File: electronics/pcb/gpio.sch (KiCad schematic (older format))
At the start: 31 parts, among them J1 Micro_SD_Card_Det_Hirose_DM3AT, J2 USB_A, J3 USB_A, J5 Conn_02x10_Odd_Even, U2 A33, Y1 24Mhz, Y2 32.768khz

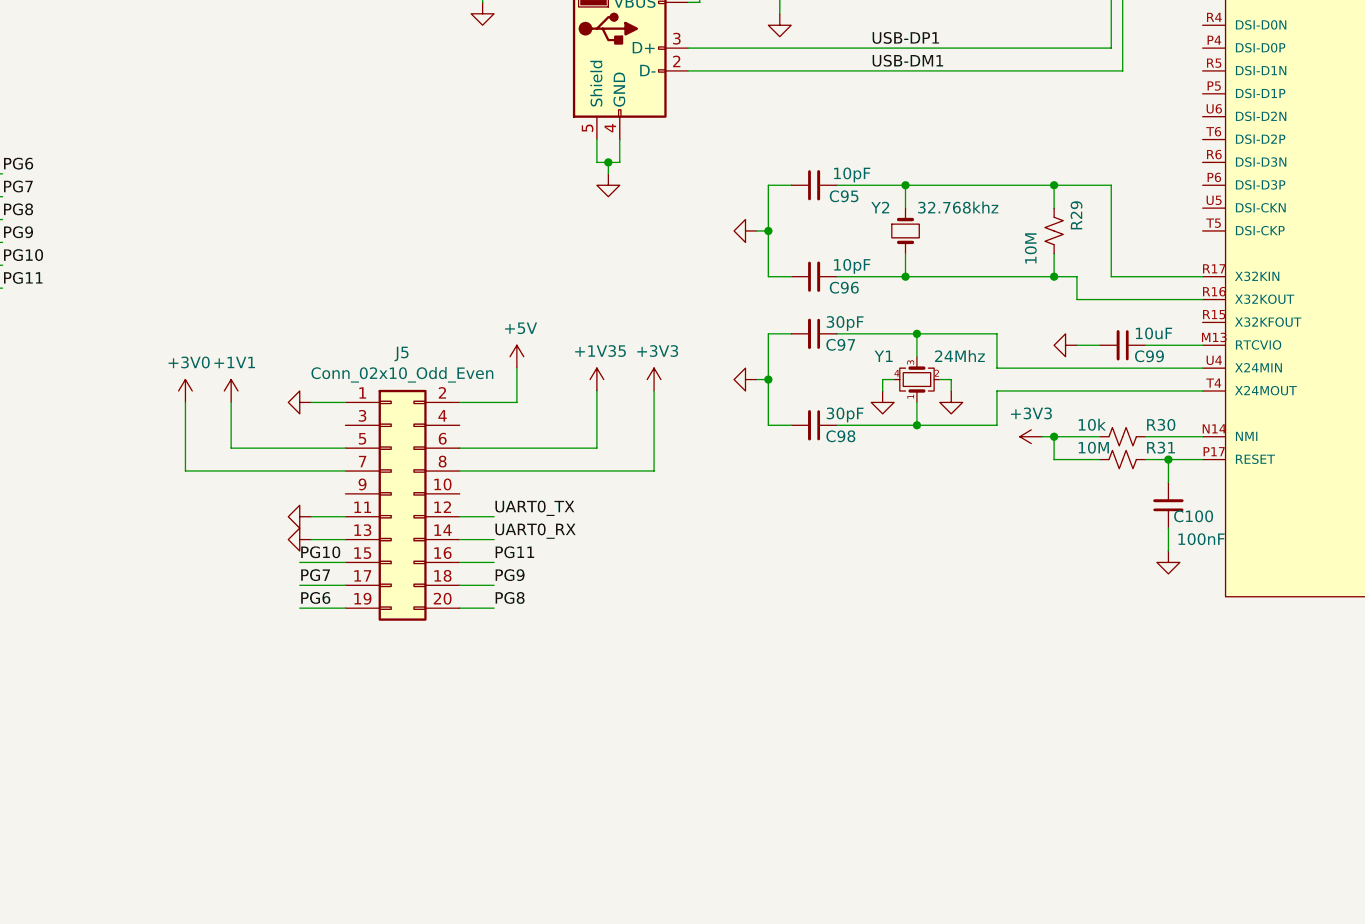
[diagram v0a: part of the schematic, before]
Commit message: Pulled out reset line
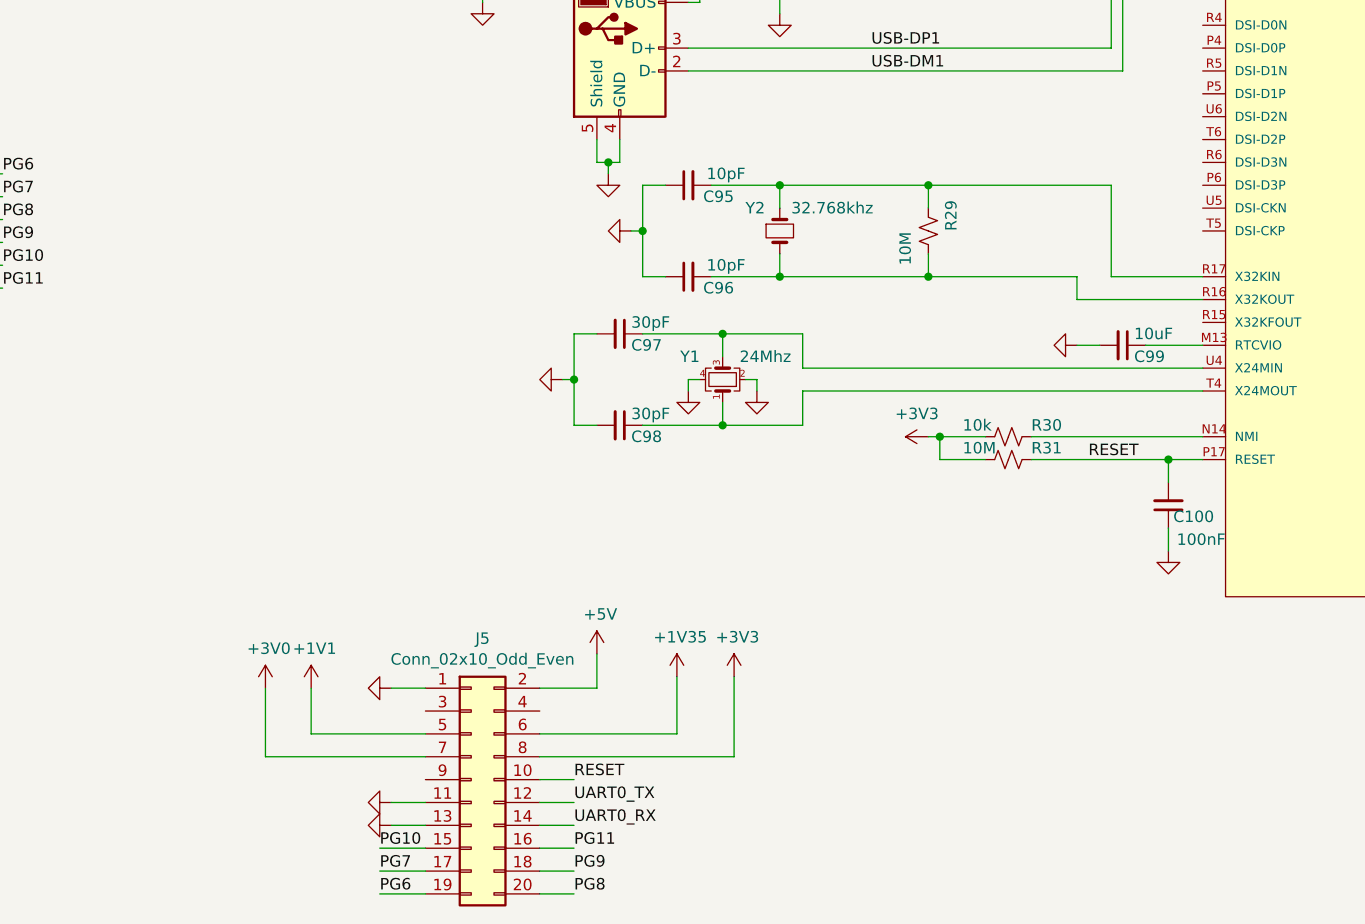
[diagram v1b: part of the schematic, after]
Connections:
- net RESET: now reaches C100.2, R31.1, U2.P17 (RESET)
- net RESET: now also J5.10 (Pin_10)
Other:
- moved on the sheet: C95, C96, C97, C98, J5, R29, R30, R31, Y1, Y2

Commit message: DRC + BOM script
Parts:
- J1: MPN (none) -> DM3AT-SF-PEJM5
- J2, J3: MPN (none) -> 1050570001; Part Number 1050570001 -> (none)
- Y1: MPN (none) -> ABM8G-24.000MHZ-18-D2Y-T; Part Number ABM8G-24.000MHZ-18-D2Y-T -> (none)
- Y2: MPN (none) -> ABS05-32.768KHZ-9-T; Part Number ABS05-32.768KHZ-9-T -> (none)
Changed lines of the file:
@@
 F 2 "Connector_Card:microSD_HC_Hirose_DM3AT-SF-PEJM5" H 12000 2150 50  0001 C CNN
 F 3 "https://www.hirose.com/product/en/download_file/key_name/DM3/category/Catalog/doc_file_id/49662/?file_category_id=4&item_id=195&is_series=1" H 9950 1550 50  0001 C CNN
+F 4 "DM3AT-SF-PEJM5" H 9950 1450 50  0001 C CNN "MPN"
 	1    9950 1450
 	1    0    0    -1
@@
 F 2 "Crystal:Crystal_SMD_Abracon_ABM8G-4Pin_3.2x2.5mm" H 5950 5050 50  0001 C CNN
 F 3 "~" H 5950 5050 50  0001 C CNN
-F 4 "ABM8G-24.000MHZ-18-D2Y-T" H 5950 5050 50  0001 C CNN "Part Number"
+F 4 "ABM8G-24.000MHZ-18-D2Y-T" H 5950 5050 50  0001 C CNN "MPN"
 	1    5950 5050
 	0    -1   -1   0
@@
 F 2 "Abracon:Abracon-ABS05-0-0-MFG" H 6200 4400 50  0001 C CNN
 F 3 "~" H 6200 4400 50  0001 C CNN
-F 4 "ABS05-32.768KHZ-9-T" H 6200 4400 50  0001 C CNN "Part Number"
+F 4 "ABS05-32.768KHZ-9-T" H 6200 4400 50  0001 C CNN "MPN"
 	1    6200 4400
 	0    1    1    0
@@
 F 2 "Connector_USB:USB_A_Molex_105057_Vertical" H 5100 2800 50  0001 C CNN
 F 3 " ~" H 5100 2800 50  0001 C CNN
-F 4 "1050570001" H 4950 2850 50  0001 C CNN "Part Number"
+F 4 "1050570001" H 4950 2850 50  0001 C CNN "MPN"
 	1    4950 2850
 	1    0    0    -1
@@
 F 2 "Connector_USB:USB_A_Molex_105057_Vertical" H 5650 3550 50  0001 C CNN
 F 3 " ~" H 5650 3550 50  0001 C CNN
-F 4 "1050570001" H 5500 3600 50  0001 C CNN "Part Number"
+F 4 "1050570001" H 5500 3600 50  0001 C CNN "MPN"
 	1    5500 3600
 	1    0    0    -1

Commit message: Removed all the extra fields
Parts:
- U2: DC Supply Voltage for I/O 1.8V ~ 3.3V -> (none); category IC -> (none); ipc land pattern name BGA289N80P17X17_1400X1400X129 -> (none); lead free yes -> (none); library id f6b937119e25c27a -> (none); manufacturer Allwinner Technology Co., Ltd. -> (none); package TFBGA282 -> (none); rohs yes -> (none); temperature range high +125°C -> (none); temperature range low -40°C -> (none)
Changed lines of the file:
@@
 F 2 "A33_FP:Allwinner_Technology_Co.,_Ltd.-A33-0" H 1650 1350 50  0001 L CNN
 F 3 "http://dl.linux-sunxi.org/A33/A33_Datasheet_release1.0.pdf" H 1650 1450 50  0001 L CNN
-F 4 "1.8V ~ 3.3V" H 1650 1550 50  0001 L CNN "DC Supply Voltage for I/O"
-F 5 "IC" H 1650 1650 50  0001 L CNN "category"
-F 6 "BGA289N80P17X17_1400X1400X129" H 1650 1750 50  0001 L CNN "ipc land pattern name"
-F 7 "yes" H 1650 1850 50  0001 L CNN "lead free"
-F 8 "f6b937119e25c27a" H 1650 1950 50  0001 L CNN "library id"
-F 9 "Allwinner Technology Co., Ltd." H 1650 2050 50  0001 L CNN "manufacturer"
-F 10 "TFBGA282" H 1650 2150 50  0001 L CNN "package"
-F 11 "yes" H 1650 2250 50  0001 L CNN "rohs"
-F 12 "+125°C" H 1650 2350 50  0001 L CNN "temperature range high"
-F 13 "-40°C" H 1650 2450 50  0001 L CNN "temperature range low"
-F 14 "" H 1650 2550 50  0001 L CNN "voltage"
 	3    1650 950
 	1    0    0    -1
@@
 F 2 "A33_FP:Allwinner_Technology_Co.,_Ltd.-A33-0" H 7950 3400 50  0001 L CNN
 F 3 "http://dl.linux-sunxi.org/A33/A33_Datasheet_release1.0.pdf" H 7950 3500 50  0001 L CNN
-F 4 "1.8V ~ 3.3V" H 7950 3600 50  0001 L CNN "DC Supply Voltage for I/O"
-F 5 "IC" H 7950 3700 50  0001 L CNN "category"
-F 6 "BGA289N80P17X17_1400X1400X129" H 7950 3800 50  0001 L CNN "ipc land pattern name"
-F 7 "yes" H 7950 3900 50  0001 L CNN "lead free"
-F 8 "f6b937119e25c27a" H 7950 4000 50  0001 L CNN "library id"
-F 9 "Allwinner Technology Co., Ltd." H 7950 4100 50  0001 L CNN "manufacturer"
-F 10 "TFBGA282" H 7950 4200 50  0001 L CNN "package"
-F 11 "yes" H 7950 4300 50  0001 L CNN "rohs"
-F 12 "+125°C" H 7950 4400 50  0001 L CNN "temperature range high"
-F 13 "-40°C" H 7950 4500 50  0001 L CNN "temperature range low"
-F 14 "" H 7950 4600 50  0001 L CNN "voltage"
 	4    7950 3000
 	1    0    0    -1

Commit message: Part numbers are _properly_ in now.
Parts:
- C100, C104, C93: MPN (none) -> CC0402KRX7R7BB104
- C101: MPN (none) -> CL05A105KO5NNNC
- C102, C103, C105, C106, C99: MPN (none) -> CL05A106MQ5NUNC
- C94: MPN (none) -> GRM155R60J226ME11D
- C95, C96: MPN (none) -> CC0402JRNPO9BN100
- C97, C98: MPN (none) -> CC0402JRNPO9BN300
- R20, R21, R23, R24, R25: MPN (none) -> CR0402-JW-104GLF
- R22, R30: MPN (none) -> RC0402JR-0710KL
- R29, R31: MPN (none) -> 0402WGJ0106TCE
- R32: MPN (none) -> RC0402FR-07200KL
- U2: MPN (none) -> A33
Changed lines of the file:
@@
 F 1 "A33" H 2200 1124 50 0000 C CNN
 F 2 "A33_FP:Allwinner_Technology_Co.,_Ltd.-A33-0" H 1650 1350 50 0001 L CNN
-F 3 "http://dl.linux-sunxi.org/A33/A33_Datasheet_release1.0.pdf" H 1650 1450 50 0001 L CNN
+F 3 "~" H 1650 1450 50 0001 L CNN
+F 4 "A33" H 2200 1315 50 0001 C CNN "MPN"
+F 5 "~" H 2200 1315 50 0001 C CNN "Tolerance"
 	3    1650 950
 	1    0    0    -1
@@
 F 1 "A33" H 8850 3174 50 0000 C CNN
 F 2 "A33_FP:Allwinner_Technology_Co.,_Ltd.-A33-0" H 7950 3400 50 0001 L CNN
-F 3 "http://dl.linux-sunxi.org/A33/A33_Datasheet_release1.0.pdf" H 7950 3500 50 0001 L CNN
+F 3 "~" H 7950 3500 50 0001 L CNN
+F 4 "A33" H 8850 3365 50 0001 C CNN "MPN"
+F 5 "~" H 8850 3365 50 0001 C CNN "Tolerance"
 	4    7950 3000
 	1    0    0    -1
@@
 F 1 "Micro_SD_Card_Det_Hirose_DM3AT" H 9900 2176 50 0000 C CNN
 F 2 "Connector_Card:microSD_HC_Hirose_DM3AT-SF-PEJM5" H 12000 2150 50 0001 C CNN
-F 3 "https://www.hirose.com/product/en/download_file/key_name/DM3/category/Catalog/doc_file_id/49662/?file_category_id=4&item_id=195&is_series=1" H 9950 1550 50 0001 C CNN
+F 3 "~" H 9950 1550 50 0001 C CNN
 F 4 "DM3AT-SF-PEJM5" H 9950 1450 50 0001 C CNN "MPN"
+F 5 "~" H 9900 2367 50 0001 C CNN "Tolerance"
 	1    9950 1450
 	1    0    0    -1
@@
 F 2 "Resistor_SMD:R_0402_1005Metric" H 8200 1650 50 0001 C CNN
 F 3 "~" H 8200 1650 50 0001 C CNN
+F 4 "CR0402-JW-104GLF" H 8150 1800 50 0001 C CNN "MPN"
+F 5 "~" H 8150 1800 50 0001 C CNN "Tolerance"
 	1    8200 1650
 	0    -1   -1   0
@@
 F 2 "Resistor_SMD:R_0402_1005Metric" H 8200 1750 50 0001 C CNN
 F 3 "~" H 8200 1750 50 0001 C CNN
+F 4 "CR0402-JW-104GLF" H 8150 1900 50 0001 C CNN "MPN"
+F 5 "~" H 8150 1900 50 0001 C CNN "Tolerance"
 	1    8200 1750
 	0    -1   -1   0
@@
 F 2 "Resistor_SMD:R_0402_1005Metric" H 8200 1150 50 0001 C CNN
 F 3 "~" H 8200 1150 50 0001 C CNN
+F 4 "CR0402-JW-104GLF" H 8150 1300 50 0001 C CNN "MPN"
+F 5 "~" H 8150 1300 50 0001 C CNN "Tolerance"
 	1    8200 1150
 	0    -1   -1   0
@@
 F 2 "Resistor_SMD:R_0402_1005Metric" H 8200 1050 50 0001 C CNN
 F 3 "~" H 8200 1050 50 0001 C CNN
+F 4 "CR0402-JW-104GLF" H 8150 1200 50 0001 C CNN "MPN"
+F 5 "~" H 8150 1200 50 0001 C CNN "Tolerance"
 	1    8200 1050
 	0    -1   -1   0
@@
 F 2 "Resistor_SMD:R_0402_1005Metric" H 8200 1250 50 0001 C CNN
 F 3 "~" H 8200 1250 50 0001 C CNN
+F 4 "RC0402JR-0710KL" H 8150 1400 50 0001 C CNN "MPN"
+F 5 "~" H 8150 1400 50 0001 C CNN "Tolerance"
 	1    8200 1250
 	0    -1   -1   0
@@
 F 2 "Resistor_SMD:R_0402_1005Metric" H 8200 1850 50 0001 C CNN
 F 3 "~" H 8200 1850 50 0001 C CNN
+F 4 "CR0402-JW-104GLF" H 8150 2000 50 0001 C CNN "MPN"
+F 5 "~" H 8150 2000 50 0001 C CNN "Tolerance"
 	1    8200 1850
 	0    -1   -1   0
@@
 F 2 "Capacitor_SMD:C_0402_1005Metric" H 7500 1300 50 0001 C CNN
 F 3 "~" H 7500 1300 50 0001 C CNN
+F 4 "CC0402KRX7R7BB104" H 7550 1450 50 0001 C CNN "MPN"
+F 5 "~" H 7550 1450 50 0001 C CNN "Tolerance"
 	1    7500 1300
 	1    0    0    -1
@@
 F 2 "Capacitor_SMD:C_0402_1005Metric" H 7700 1300 50 0001 C CNN
 F 3 "~" H 7700 1300 50 0001 C CNN
+F 4 "GRM155R60J226ME11D" H 7750 1450 50 0001 C CNN "MPN"
+F 5 "~" H 7750 1450 50 0001 C CNN "Tolerance"
 	1    7700 1300
 	1    0    0    -1
@@
 F 3 "~" H 5950 5050 50 0001 C CNN
 F 4 "ABM8G-24.000MHZ-18-D2Y-T" H 5950 5050 50 0001 C CNN "MPN"
+F 5 "~" H 6050 5250 50 0001 C CNN "Tolerance"
 	1    5950 5050
 	0    -1   -1   0
@@
 F 3 "~" H 6200 4400 50 0001 C CNN
 F 4 "ABS05-32.768KHZ-9-T" H 6200 4400 50 0001 C CNN "MPN"
+F 5 "~" H 6100 4350 50 0001 C CNN "Tolerance"
 	1    6200 4400
 	0    1    1    0
@@
 F 2 "Capacitor_SMD:C_0402_1005Metric" H 5500 4850 50 0001 C CNN
 F 3 "~" H 5500 4850 50 0001 C CNN
+F 4 "CC0402JRNPO9BN300" H 5550 5000 50 0001 C CNN "MPN"
+F 5 "~" H 5550 5000 50 0001 C CNN "Tolerance"
 	1    5500 4850
 	0    1    1    0
@@
 F 2 "Capacitor_SMD:C_0402_1005Metric" H 5500 5250 50 0001 C CNN
 F 3 "~" H 5500 5250 50 0001 C CNN
+F 4 "CC0402JRNPO9BN300" H 5550 5400 50 0001 C CNN "MPN"
+F 5 "~" H 5550 5400 50 0001 C CNN "Tolerance"
 	1    5500 5250
 	0    1    1    0
@@
 F 2 "Capacitor_SMD:C_0402_1005Metric" H 5800 4600 50 0001 C CNN
 F 3 "~" H 5800 4600 50 0001 C CNN
+F 4 "CC0402JRNPO9BN100" H 5750 4500 50 0001 C CNN "MPN"
+F 5 "~" H 5750 4500 50 0001 C CNN "Tolerance"
 	1    5800 4600
 	0    -1   -1   0
@@
 F 2 "Capacitor_SMD:C_0402_1005Metric" H 5800 4200 50 0001 C CNN
 F 3 "~" H 5800 4200 50 0001 C CNN
+F 4 "CC0402JRNPO9BN100" H 5750 4100 50 0001 C CNN "MPN"
+F 5 "~" H 5750 4100 50 0001 C CNN "Tolerance"
 	1    5800 4200
 	0    -1   -1   0
@@
 F 2 "Resistor_SMD:R_0402_1005Metric" H 6850 4400 50 0001 C CNN
 F 3 "~" H 6850 4400 50 0001 C CNN
+F 4 "0402WGJ0106TCE" H 6950 4500 50 0001 C CNN "MPN"
+F 5 "~" H 6950 4500 50 0001 C CNN "Tolerance"
 	1    6850 4400
 	1    0    0    -1
@@
 F 2 "Capacitor_SMD:C_0402_1005Metric" H 7700 4900 50 0001 C CNN
 F 3 "~" H 7700 4900 50 0001 C CNN
+F 4 "CL05A106MQ5NUNC" H 7750 5050 50 0001 C CNN "MPN"
+F 5 "~" H 7750 5050 50 0001 C CNN "Tolerance"
 	1    7700 4900
 	0    1    1    0
@@
 F 2 "Resistor_SMD:R_0402_1005Metric" H 7200 5300 50 0001 C CNN
 F 3 "~" H 7200 5300 50 0001 C CNN
+F 4 "RC0402JR-0710KL" H 7150 5500 50 0001 C CNN "MPN"
+F 5 "~" H 7150 5500 50 0001 C CNN "Tolerance"
 	1    7200 5300
 	0    1    1    0
@@
 F 2 "Resistor_SMD:R_0402_1005Metric" H 7200 5400 50 0001 C CNN
 F 3 "~" H 7200 5400 50 0001 C CNN
+F 4 "0402WGJ0106TCE" H 7150 5600 50 0001 C CNN "MPN"
+F 5 "~" H 7150 5600 50 0001 C CNN "Tolerance"
 	1    7200 5400
 	0    1    1    0
@@
 F 2 "Capacitor_SMD:C_0402_1005Metric" H 7900 5600 50 0001 C CNN
 F 3 "~" H 7900 5600 50 0001 C CNN
+F 4 "CC0402KRX7R7BB104" H 7700 5750 50 0001 C CNN "MPN"
+F 5 "~" H 7700 5750 50 0001 C CNN "Tolerance"
 	1    7900 5600
 	-1   0    0    1
@@
 F 2 "Capacitor_SMD:C_0402_1005Metric" H 10050 5700 50 0001 C CNN
 F 3 "~" H 10050 5700 50 0001 C CNN
+F 4 "CL05A105KO5NNNC" H 10100 5550 50 0001 C CNN "MPN"
+F 5 "~" H 10100 5550 50 0001 C CNN "Tolerance"
 	1    10050 5700
 	0    -1   -1   0
@@
 F 2 "Capacitor_SMD:C_0402_1005Metric" H 10050 5850 50 0001 C CNN
 F 3 "~" H 10050 5850 50 0001 C CNN
+F 4 "CL05A106MQ5NUNC" H 10100 5700 50 0001 C CNN "MPN"
+F 5 "~" H 10100 5700 50 0001 C CNN "Tolerance"
 	1    10050 5850
 	0    -1   -1   0
@@
 F 2 "Capacitor_SMD:C_0402_1005Metric" H 10050 6050 50 0001 C CNN
 F 3 "~" H 10050 6050 50 0001 C CNN
+F 4 "CL05A106MQ5NUNC" H 10100 5900 50 0001 C CNN "MPN"
+F 5 "~" H 10100 5900 50 0001 C CNN "Tolerance"
 	1    10050 6050
 	0    -1   -1   0
@@
 F 2 "Capacitor_SMD:C_0402_1005Metric" H 10050 6200 50 0001 C CNN
 F 3 "~" H 10050 6200 50 0001 C CNN
+F 4 "CC0402KRX7R7BB104" H 10100 6050 50 0001 C CNN "MPN"
+F 5 "~" H 10100 6050 50 0001 C CNN "Tolerance"
 	1    10050 6200
 	0    -1   -1   0
@@
 F 2 "Resistor_SMD:R_0402_1005Metric" H 10500 5950 50 0001 C CNN
 F 3 "~" H 10500 5950 50 0001 C CNN
+F 4 "RC0402FR-07200KL" H 10450 6100 50 0001 C CNN "MPN"
+F 5 "~" H 10450 6100 50 0001 C CNN "Tolerance"
 	1    10500 5950
 	0    1    1    0
@@
 F 1 "USB_A" H 5007 3226 50 0000 C CNN
 F 2 "Connector_USB:USB_A_Molex_105057_Vertical" H 5100 2800 50 0001 C CNN
-F 3 " ~" H 5100 2800 50 0001 C CNN
+F 3 "~" H 5100 2800 50 0001 C CNN
 F 4 "1050570001" H 4950 2850 50 0001 C CNN "MPN"
+F 5 "~" H 5007 3417 50 0001 C CNN "Tolerance"
 	1    4950 2850
 	1    0    0    -1
@@
 F 1 "USB_A" H 5557 3976 50 0000 C CNN
 F 2 "Connector_USB:USB_A_Molex_105057_Vertical" H 5650 3550 50 0001 C CNN
-F 3 " ~" H 5650 3550 50 0001 C CNN
+F 3 "~" H 5650 3550 50 0001 C CNN
 F 4 "1050570001" H 5500 3600 50 0001 C CNN "MPN"
+F 5 "~" H 5557 4167 50 0001 C CNN "Tolerance"
 	1    5500 3600
 	1    0    0    -1
@@
 F 2 "Capacitor_SMD:C_0402_1005Metric" H 5450 2550 50 0001 C CNN
 F 3 "~" H 5450 2550 50 0001 C CNN
+F 4 "CL05A106MQ5NUNC" H 5500 2700 50 0001 C CNN "MPN"
+F 5 "~" H 5500 2700 50 0001 C CNN "Tolerance"
 	1    5450 2550
 	0    1    1    0
@@
 F 2 "Capacitor_SMD:C_0402_1005Metric" H 6000 3300 50 0001 C CNN
 F 3 "~" H 6000 3300 50 0001 C CNN
+F 4 "CL05A106MQ5NUNC" H 6050 3450 50 0001 C CNN "MPN"
+F 5 "~" H 6050 3450 50 0001 C CNN "Tolerance"
 	1    6000 3300
 	0    1    1    0
@@
 F 2 "Connector_PinHeader_2.54mm:PinHeader_2x10_P2.54mm_Vertical" H 4850 6800 50 0001 C CNN
 F 3 "~" H 4850 6800 50 0001 C CNN
+F 4 "~" H 4900 7517 50 0001 C CNN "Tolerance"
 	1    4850 6800
 	1    0    0    -1
